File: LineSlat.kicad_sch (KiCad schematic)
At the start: 128 parts, among them J4 DEBUG, J5 RJ45, J6 RJ45, J7 USB_B_Micro, J8 BATT, Q1 DMG3402, Q10 MMBT3904L, Q12 DMN6075S, Q13 MMBT3906, Q2 DMG3402, Q3 DMG3402, Q4 DMG3402, Q5 DMG3402, Q6 DMG3402, Q7 DMP3099L, Q8 MMBT3904L, Q9 DMN6075S, SW1 SPDT, SW2 SPDT, SW3 RESET, U1 THVD1400D, U2 THVD1400D, U3 RFM95W-915S2, U4 ATSAMD21G18A-A, U5 TSR1-2433E, Y1 32.768K-12.5p

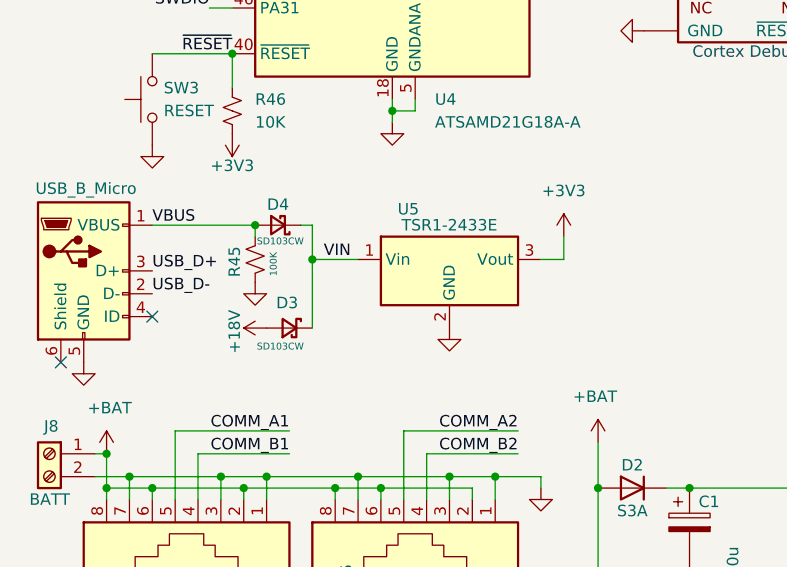
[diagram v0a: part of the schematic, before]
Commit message: Change diodes and regulator
Changed regulator from TSR-1-2433E to TSR-1-2433
This changes Vin minimum from 6V to 4.76V

Changed schottky diodes to BAT54W.
This fixes 2 issues:
- reverse voltage 20V -> 30V (not enough margin for ~20V LiPo)
- forward voltage drop 600mV -> 250mV (5V-600mV is below Vin min of 3.3V regulator)
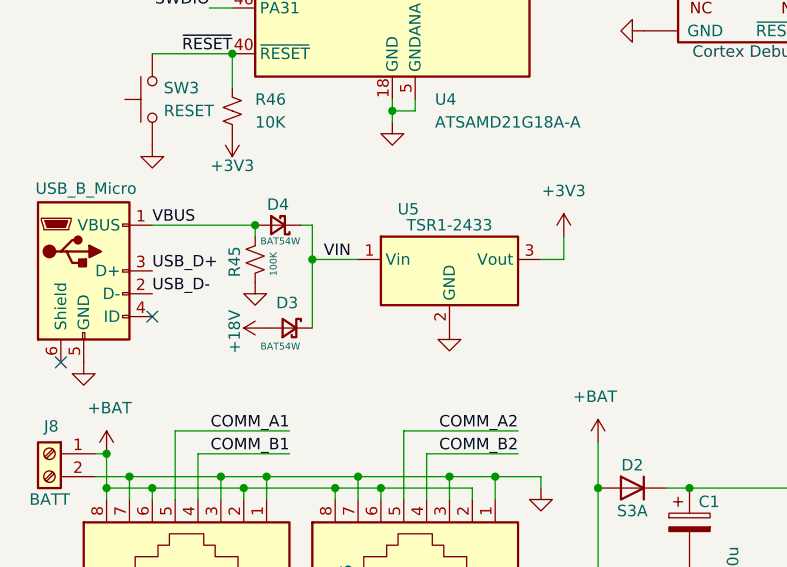
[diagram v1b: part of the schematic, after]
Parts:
- D3, D4: value SD103CW -> BAT54W; Mouser Part Number 78-SD103CW-HE3_A-08 -> 78-BAT54W-HG3-18
- U5: value TSR1-2433E -> TSR1-2433
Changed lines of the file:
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@@
 			)
 		)
-		(property "Value" "SD103CW"
+		(property "Value" "BAT54W"
 			(at 40.894 146.558 0)
 			(effects
@@
 			)
 		)
-		(property "Mouser Part Number" "78-SD103CW-HE3_A-08 "
+		(property "Mouser Part Number" "78-BAT54W-HG3-18 "
 			(at 40.64 144.78 0)
 			(effects
@@
 			)
 		)
-		(property "Value" "SD103CW"
+		(property "Value" "BAT54W"
 			(at 40.894 158.242 0)
 			(effects
@@
 			)
 		)
-		(property "Mouser Part Number" "78-SD103CW-HE3_A-08 "
+		(property "Mouser Part Number" "78-BAT54W-HG3-18 "
 			(at 41.91 156.21 0)
 			(effects
@@
 			)
 		)
-		(property "Value" "TSR1-2433E"
+		(property "Value" "TSR1-2433"
 			(at 59.69 144.78 0)
 			(effects
@@
 			)
 		)
-		(property "Datasheet" "https://www.tracopower.com/products/tsr1e.pdf"
+		(property "Datasheet" "https://www.tracopower.com/products/tsr1.pdf"
 			(at 59.69 154.94 0)
 			(effects

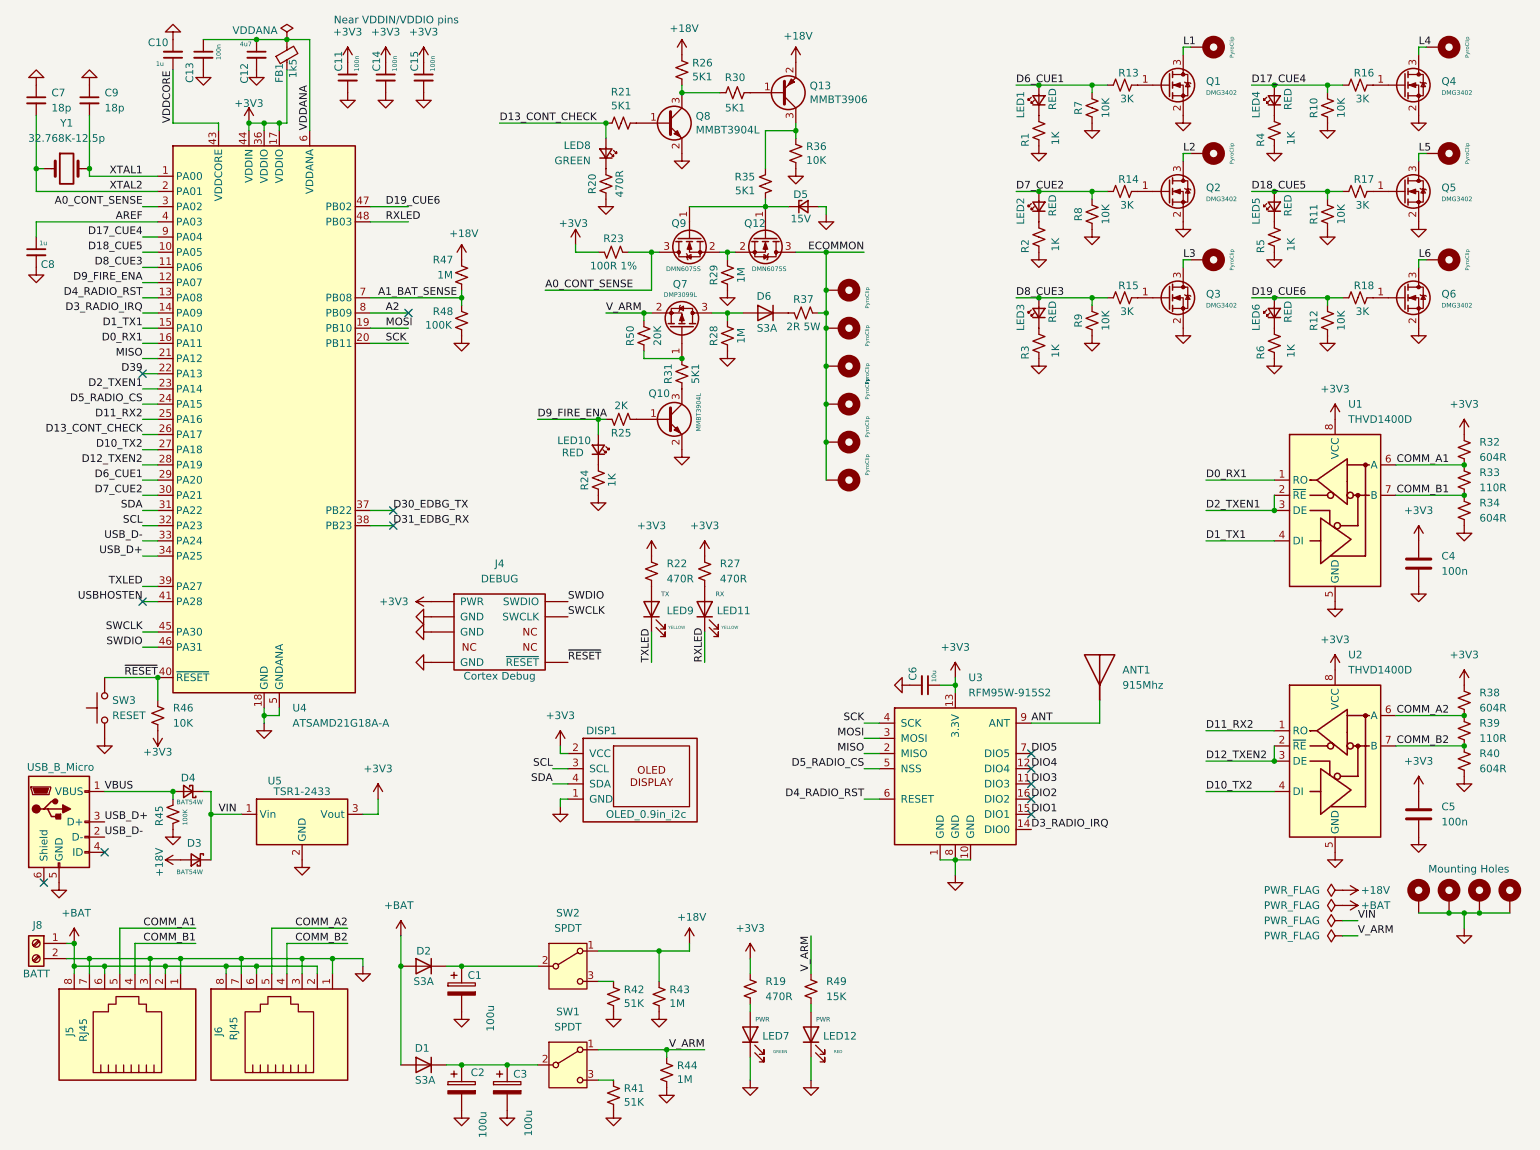
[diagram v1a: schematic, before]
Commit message: v2.0
* new continuity test using INA219
* 8 cues instead of 6
* Lots of minor changes
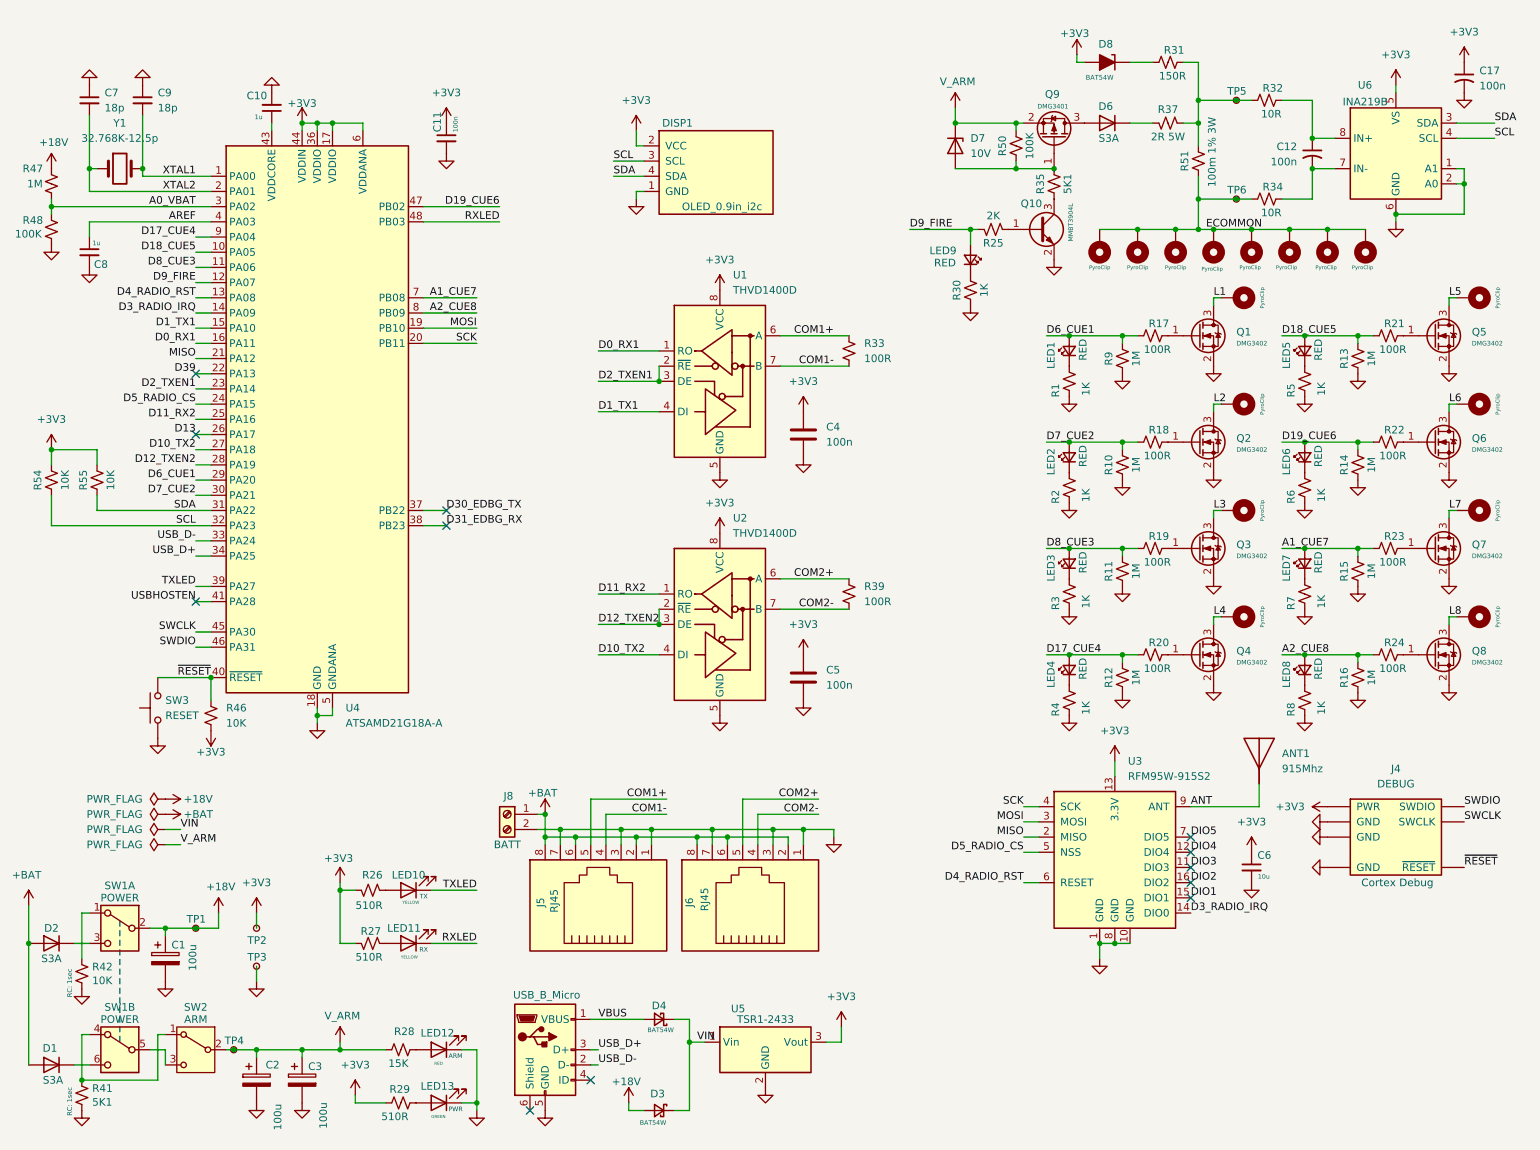
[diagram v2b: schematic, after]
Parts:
- removed ANT1: 915Mhz, RF_Antenna:Texas_SWRA416_868MHz_915MHz, symbol MyLib:Antenna915MhzPCBCoil
- removed C12: 4u7, Capacitor_SMD:C_0805_2012Metric, symbol Device:C_Small
- removed C13, C14, C15: 100n, Capacitor_SMD:C_0805_2012Metric, symbol Device:C_Small
- removed D5: 15V, MyLib:D_SOT-23_ANK, symbol Device:D_Zener_Small
- removed FB1: 1k5, Inductor_SMD:L_0805_2012Metric, symbol Device:FerriteBead_Small
- removed H1, H2, H3, H4: MountingHole, MountingHole:MountingHole_3.2mm_M3_ISO7380_Pad, symbol Mechanical:MountingHole_Pad
- removed Q12, Q9: DMN6075S, Package_TO_SOT_SMD:SOT-23, symbol MyLib:DMG3402
- removed Q13: MMBT3906, Package_TO_SOT_SMD:SOT-23, symbol Transistor_BJT:MMBT3906
- removed Q8: MMBT3904L, Package_TO_SOT_SMD:SOT-23, symbol Transistor_BJT:MMBT3904
- removed R20: 470R, Resistor_SMD:R_0805_2012Metric, symbol Device:R_Small_US
- removed R21, R26, R30, R35: 5K1, Resistor_SMD:R_0805_2012Metric, symbol Device:R_Small_US
- removed R28, R29, R43, R44: 1M, Resistor_SMD:R_0805_2012Metric, symbol Device:R_Small_US
- removed R36: 10K, Resistor_SMD:R_0805_2012Metric, symbol Device:R_Small_US
- removed R38, R40: 604R, Resistor_SMD:R_0805_2012Metric, symbol Device:R_Small_US
- removed R45: 100K, Resistor_SMD:R_0805_2012Metric, symbol Device:R_Small_US
- removed SW1, SW2: SPDT, MyLib:spdt_100SP1T1B2M2QE, symbol Switch:SW_SPDT
- added ANT1: 915Mhz, MyLib:Antenna915MHzSimpleCoil, symbol MyLib:Antenna915MhzSimpleCoil
- added C12, C17: 100n, Capacitor_SMD:C_0603_1608Metric, symbol Device:C_Small_US
- added CLIP15, CLIP16: PyroClip, MyLib:PyroClipRed, symbol MyLib:PyroClipRed
- added CLIP7, CLIP8: PyroClip, MyLib:PyroClipBlack, symbol MyLib:PyroClipBlack
- added D7: 10V, Package_TO_SOT_SMD:SOT-23, symbol Diode:BZX84Cxx
- added D8: BAT54W, Diode_SMD:D_SOD-123, symbol MyLib:BAT54W
- added LED7: RED, LED_SMD:LED_0805_2012Metric, symbol Device:LED_Small
- added Q7, Q8: DMG3402, Package_TO_SOT_SMD:SOT-23, symbol MyLib:DMG3402
- added R15, R16: 1M, Resistor_SMD:R_0603_1608Metric, symbol Device:R_Small_US
- added R24: 100R, Resistor_SMD:R_0603_1608Metric, symbol Device:R_Small_US
- added R31: 150R, Resistor_SMD:R_0603_1608Metric, symbol Device:R_Small_US
- added R51: 100m 1% 3W, Resistor_SMD:R_2512_6332Metric, symbol Device:R_Small_US
- added R54, R55: 10K, Resistor_SMD:R_0603_1608Metric, symbol Device:R_Small_US
- added R7, R8: 1K, Resistor_SMD:R_0603_1608Metric, symbol Device:R_Small_US
- added SW1: POWER, MyLib:DPDT-SW-T2-4E-B-A2-MA2, symbol MyLib:DPDT-SW-T2-4E-B-A2-MA2
- added SW2: ARM, MyLib:SPDT-SW-T2-2E-A-A2-M1, symbol MyLib:SPDT-SW-T2-2E-A-A2-M1
- added TP1, TP2, TP3, TP4, TP5, TP6: RCTCTE, MyLib:RCTCTE, symbol MyLib:RCTCTE
- added U6: INA219B, Package_SO:SOIC-8_3.9x4.9mm_P1.27mm, symbol Sensor_Energy:INA219BxD
- C1, C2, C3: Mouser Part Number 710-860010573007 -> (none); Mouser_Part_Number (none) -> 710-860010573007
- C10, C8: footprint Capacitor_SMD:C_0805_2012Metric -> Capacitor_SMD:C_0603_1608Metric; Mouser Part Number 710-885012207022 -> (none)
- C11, C4, C5: footprint Capacitor_SMD:C_0805_2012Metric -> Capacitor_SMD:C_0603_1608Metric; Mouser Part Number 80-C0805C104M5RACTM -> (none)
- C6: footprint Capacitor_SMD:C_0805_2012Metric -> Capacitor_SMD:C_0603_1608Metric; Mouser Part Number LMK212AC6106KD-T -> (none)
- C7, C9: footprint Capacitor_SMD:C_0805_2012Metric -> Capacitor_SMD:C_0603_1608Metric; Mouser Part Number 80-C0805C180J5GAC -> (none)
- CLIP1, CLIP2, CLIP3, CLIP4, CLIP5, CLIP6: Datasheet2 https://www.pyromate.com/quick-clip.htm -> (none); Mouser Part Number N/A -> (none); Mouser_Part_Number (none) -> N/A
- CLIP10: renamed from CLIP11; Datasheet2 https://www.pyromate.com/quick-clip.htm -> (none); Mouser Part Number N/A -> (none); Mouser_Part_Number (none) -> N/A
- CLIP11: renamed from CLIP10; Datasheet2 https://www.pyromate.com/quick-clip.htm -> (none); Mouser Part Number N/A -> (none); Mouser_Part_Number (none) -> N/A
- CLIP12: renamed from CLIP9; Datasheet2 https://www.pyromate.com/quick-clip.htm -> (none); Mouser Part Number N/A -> (none); Mouser_Part_Number (none) -> N/A
- CLIP13: renamed from CLIP8; Datasheet2 https://www.pyromate.com/quick-clip.htm -> (none); Mouser Part Number N/A -> (none); Mouser_Part_Number (none) -> N/A
- CLIP14: renamed from CLIP7; Datasheet2 https://www.pyromate.com/quick-clip.htm -> (none); Mouser Part Number N/A -> (none); Mouser_Part_Number (none) -> N/A
- CLIP9: renamed from CLIP12; Datasheet2 https://www.pyromate.com/quick-clip.htm -> (none); Mouser Part Number N/A -> (none); Mouser_Part_Number (none) -> N/A
- D1, D2, D6: Mouser Part Number 512-S3A -> (none); Mouser_Part_Number (none) -> 512-S3A
- D3, D4: Mouser Part Number 78-BAT54W-HG3-18 -> (none); Mouser_Part_Number (none) -> 78-BAT54W-HG3-18
- DISP1: Mouser Part Number N/A -> (none); Mouser_Part_Number (none) -> N/A
- J4: Mouser Part Number 640-BD12510A305580LB -> (none); Mouser_Part_Number (none) -> 640-BD12510A305580LB
- J5, J6: Mouser Part Number 530-SS-700810-NF -> (none); Mouser_Part_Number (none) -> 530-SS-700810-NF
- J7: Mouser Part Number 649-10118194-0011LF -> (none); Mouser_Part_Number (none) -> 649-10118194-0011LF
- J8: symbol Connector:Screw_Terminal_01x02 -> MyLib:Screw_Terminal_01x02_P5.08mm; Mouser Part Number 649-VI02215200J0G -> (none); Mouser_Part_Number (none) -> 649-VI02215200J0G
- LED1, LED12, LED2, LED3, LED4, LED5, LED6: Mouser Part Number 710-150080RS75000 -> (none); Mouser_Part_Number (none) -> 710-150080RS75000
- LED10: renamed from LED9; Mouser Part Number 710-150080YS75000 -> (none); Mouser_Part_Number (none) -> 710-150080YS75000
- LED11: Mouser Part Number 710-150080YS75000 -> (none); Mouser_Part_Number (none) -> 710-150080YS75000
- LED13: renamed from LED7; Mouser Part Number 710-150080RS75000 -> (none); Mouser_Part_Number (none) -> 710-150080RS75000
- LED8: value GREEN -> RED; Mouser Part Number 710-150080RS75000 -> (none); Mouser_Part_Number (none) -> 710-150080RS75000
- LED9: renamed from LED10; Mouser Part Number 710-150080RS75000 -> (none); Mouser_Part_Number (none) -> 710-150080RS75000
- Q1, Q2, Q3, Q4, Q5, Q6: Mouser Part Number 621-DMG3402L-7 -> (none); Mouser_Part_Number (none) -> 621-DMG3402L-7
- Q10: Mouser Part Number 771-MMBT3904VL -> (none); Mouser_Part_Number (none) -> 771-MMBT3904VL
- Q9: renamed from Q7; value DMP3099L -> DMG3401; footprint Package_TO_SOT_SMD:SOT-23 -> MyLib:SC-59; Mouser Part Number 621-DMP3099L-13 -> (none); Mouser_Part_Number (none) -> 621-DMP3099L-13
- R1, R2, R3, R4, R5, R6: footprint Resistor_SMD:R_0805_2012Metric -> Resistor_SMD:R_0603_1608Metric; Mouser Part Number 71-CRCW08051K00FKEC -> (none)
- R10: renamed from R8; value 10K -> 1M; footprint Resistor_SMD:R_0805_2012Metric -> Resistor_SMD:R_0603_1608Metric; Mouser Part Number 71-CRCW0805-10K-E3 -> (none)
- R11: renamed from R9; value 10K -> 1M; footprint Resistor_SMD:R_0805_2012Metric -> Resistor_SMD:R_0603_1608Metric; Mouser Part Number 71-CRCW0805-10K-E3 -> (none)
- R12: renamed from R10; value 10K -> 1M; footprint Resistor_SMD:R_0805_2012Metric -> Resistor_SMD:R_0603_1608Metric; Mouser Part Number 71-CRCW0805-10K-E3 -> (none)
- R13: renamed from R11; value 10K -> 1M; footprint Resistor_SMD:R_0805_2012Metric -> Resistor_SMD:R_0603_1608Metric; Mouser Part Number 71-CRCW0805-10K-E3 -> (none)
- R14: renamed from R12; value 10K -> 1M; footprint Resistor_SMD:R_0805_2012Metric -> Resistor_SMD:R_0603_1608Metric; Mouser Part Number 71-CRCW0805-10K-E3 -> (none)
- R17: renamed from R13; value 3K -> 100R; footprint Resistor_SMD:R_0805_2012Metric -> Resistor_SMD:R_0603_1608Metric; Mouser Part Number 652-CR0805JW-302ELF -> (none)
- R18: renamed from R14; value 3K -> 100R; footprint Resistor_SMD:R_0805_2012Metric -> Resistor_SMD:R_0603_1608Metric; Mouser Part Number 652-CR0805JW-302ELF -> (none)
- R19: renamed from R15; value 3K -> 100R; footprint Resistor_SMD:R_0805_2012Metric -> Resistor_SMD:R_0603_1608Metric; Mouser Part Number 652-CR0805JW-302ELF -> (none)
- R20: renamed from R16; value 3K -> 100R; footprint Resistor_SMD:R_0805_2012Metric -> Resistor_SMD:R_0603_1608Metric; Mouser Part Number 652-CR0805JW-302ELF -> (none)
- R21: renamed from R17; value 3K -> 100R; footprint Resistor_SMD:R_0805_2012Metric -> Resistor_SMD:R_0603_1608Metric; Mouser Part Number 652-CR0805JW-302ELF -> (none)
- R22: renamed from R18; value 3K -> 100R; footprint Resistor_SMD:R_0805_2012Metric -> Resistor_SMD:R_0603_1608Metric; Mouser Part Number 652-CR0805JW-302ELF -> (none)
- R23: value 100R 1% -> 100R; footprint Resistor_SMD:R_0805_2012Metric -> Resistor_SMD:R_0603_1608Metric; Mouser Part Number 603-RT0805FRE07100RL -> (none)
- R25: footprint Resistor_SMD:R_0805_2012Metric -> Resistor_SMD:R_0603_1608Metric; Mouser Part Number 652-CR0805JW-202ELF -> (none)
- R26: renamed from R22; value 470R -> 510R; footprint Resistor_SMD:R_0805_2012Metric -> Resistor_SMD:R_0603_1608Metric; Mouser Part Number 71-CRCW0805-470-E3 -> (none)
- R27: value 470R -> 510R; footprint Resistor_SMD:R_0805_2012Metric -> Resistor_SMD:R_0603_1608Metric; Mouser Part Number 71-CRCW0805-470-E3 -> (none)
- R28: renamed from R49; footprint Resistor_SMD:R_0805_2012Metric -> Resistor_SMD:R_0603_1608Metric; Mouser Part Number 71-CRCW0805-15K-E3 -> (none)
- R29: renamed from R19; value 470R -> 510R; footprint Resistor_SMD:R_0805_2012Metric -> Resistor_SMD:R_0603_1608Metric; Mouser Part Number 71-CRCW0805-470-E3 -> (none)
- R30: renamed from R24; footprint Resistor_SMD:R_0805_2012Metric -> Resistor_SMD:R_0603_1608Metric; Mouser Part Number 71-CRCW08051K00FKEC -> (none)
- R32, R34: value 604R -> 10R; footprint Resistor_SMD:R_0805_2012Metric -> Resistor_SMD:R_0603_1608Metric; Mouser Part Number 603-RC0805FR-07604RL -> (none)
- R33, R39: value 110R -> 100R; footprint Resistor_SMD:R_0805_2012Metric -> Resistor_SMD:R_0603_1608Metric; Mouser Part Number 652-CR0805JW-111ELF -> (none)
- R35: renamed from R31; footprint Resistor_SMD:R_0805_2012Metric -> Resistor_SMD:R_0603_1608Metric; Mouser Part Number 71-CRCW08055K10JNEB -> (none)
- R37: Mouser Part Number 588-TUW5J2R0E -> (none); Mouser_Part_Number (none) -> 588-TUW5J2R0E
- R41: value 51K -> 5K1; footprint Resistor_SMD:R_0805_2012Metric -> Resistor_SMD:R_0603_1608Metric; Mouser Part Number 71-CRCW08055K10JNEB -> (none)
- R42: value 51K -> 10K; footprint Resistor_SMD:R_0805_2012Metric -> Resistor_SMD:R_0603_1608Metric; Mouser Part Number 71-CRCW08055K10JNEB -> (none)
- R46: footprint Resistor_SMD:R_0805_2012Metric -> Resistor_SMD:R_0603_1608Metric; Mouser Part Number 71-CRCW0805-10K-E3 -> (none)
- R47: footprint Resistor_SMD:R_0805_2012Metric -> Resistor_SMD:R_0603_1608Metric; Mouser Part Number 652-CHV0805FX1004ELF -> (none)
- R48: footprint Resistor_SMD:R_0805_2012Metric -> Resistor_SMD:R_0603_1608Metric; Mouser Part Number 652-CR0805JW-104ELF -> (none)
- R50: value 20K -> 100K; footprint Resistor_SMD:R_0805_2012Metric -> Resistor_SMD:R_0603_1608Metric; Mouser Part Number 652-CR0805JW-203ELF -> (none)
- R9: renamed from R7; value 10K -> 1M; footprint Resistor_SMD:R_0805_2012Metric -> Resistor_SMD:R_0603_1608Metric; Mouser Part Number 71-CRCW0805-10K-E3 -> (none)
- SW3: Mouser Part Number 652-CR0805JW-104ELF -> (none); Mouser_Part_Number (none) -> 652-CR0805JW-104ELF
- U1, U2: Mouser Part Number 595-THVD1400DR -> (none); Mouser_Part_Number (none) -> 595-THVD1400DR
- U3: Mouser Part Number 223-RFM95W-915S2 -> (none); Mouser_Part_Number (none) -> 223-RFM95W-915S2
- U4: Mouser Part Number 556-ATSAMD21G18A-MU -> (none); Mouser_Part_Number (none) -> 556-ATSAMD21G18A-MU
- U5: footprint Converter_DCDC:Converter_DCDC_TRACO_TSR1-xxxxE_THT -> Converter_DCDC:Converter_DCDC_TRACO_TSR-1_THT; symbol Regulator_Switching:TSR1-2433E -> Regulator_Switching:TSR_1-2433; Mouser Part Number 495-TSR-1-2433 -> (none); Mouser_Part_Number (none) -> 495-TSR-1-2433
- Y1: Mouser Part Number 520-327-12.5-34B -> (none); Mouser_Part_Number (none) -> 520-327-12.5-34B
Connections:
- net VDDANA is gone; now on net +3V3: U4.6 (VDDANA)
- net +18V: now also C1.1, SW1.2 (B), TP1.1
- net +3V3: now also C17.1, D8.2 (A), R54.2, R55.2, TP2.1, U6.5 (VS); no longer R23.2, R32.1
- net ANT: now also ANT1.1 (A)
- net ECOMMON: now also R34.1, CLIP15.1, CLIP16.1, R51.1, TP6.1; no longer R37.1
- net GND: now also C17.2, Q7.2 (S), Q8.2 (S), R15.1, R16.1, R7.1, R8.1, TP3.1, U6.1 (A1), U6.2 (A0), U6.6 (GND); no longer R34.2
- net SCL: now also R54.1, U6.4 (SCL)
- net SDA: now also R55.1, U6.3 (SDA)
- net V_ARM: now also C2.1, C3.1, D7.3 (K), SW2.2 (B), TP4.1
- net at R41.2: now also SW1.4 (A), SW2.1 (A)
- net at Q9.1 (G), R35.2, R50.1: now also D7.1 (A)
- net at LED8.1 (K): now also R8.2
- net at D2.1 (K): now also SW1.3 (C); no longer C1.1
- net at R42.2: now also SW1.1 (A)
- net A0_CONT_SENSE renamed A0_VBAT
- net A0_VBAT: now also R47.2, R48.1; no longer R23.1
- removed net A1_BAT_SENSE: R47.2, R48.1, U4.7 (PB08)
- net A2 renamed A2_CUE8
- net A2_CUE8: now also LED8.2 (A), R16.2, R24.1
- net COMM_A1 renamed COM1+
- net COM1+: no longer R32.2
- net COMM_A2 renamed COM2+
- net COMM_B1 renamed COM1-
- net COM1-: no longer R34.1
- net COMM_B2 renamed COM2-
- net D13_CONT_CHECK renamed D13
- net D13: no longer LED8.2 (A)
- net D9_FIRE_ENA renamed D9_FIRE
- net VDDCORE: no longer names the net of C10.1, U4.43 (VDDCORE)
- new net: D8.1 (K), R31.1
- new net: C12.1, R32.2, U6.8 (IN+)
- new net: C12.2, R34.2, U6.7 (IN-)
- new net: SW1.5 (B), SW2.3 (C)
- new net: D1.1 (K), SW1.6 (C)
- new net: Q8.1 (G), R24.2
- new net: R31.2, R32.1, R37.1, R51.2, TP5.1
- new net: Q7.1 (G), R23.2
- new net: LED7.1 (K), R7.2
- new net A1_CUE7: LED7.2 (A), R15.2, R23.1, U4.7 (PB08)
- new net L7: CLIP7.1, Q7.3 (D)
- new net L8: CLIP8.1, Q8.3 (D)
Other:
- note added: "ARM"
- note added: "RC: 1sec"
- note removed: "Mounting Holes"
- note removed: "Near VDDIN/VDDIO pins"
- moved on the sheet: C1, C10, C11, C2, C3, C4, C5, C6, C7, C8, C9, D1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

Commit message: Added files for 3d printed boxes using openscad
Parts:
- R29: value 510R -> 2K
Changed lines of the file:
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@@
 			)
 		)
-		(property "Value" "510R"
+		(property "Value" "2K"
 			(at 77.47 199.136 90)
 			(effects
